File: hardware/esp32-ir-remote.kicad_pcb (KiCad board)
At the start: 2 copper layers, 65 parts, among them J1 ESP32-WROOM-32E-Breakout, J2 USB_C_Receptacle_USB2.0_14P, Q1 Q_NPN_BCE, Q2 Q_NPN_BCE, Q3 IRLML6344, Q4 2N7002, Q5 2N7002, SW1 RESET, SW2 BOOT, U1 AP63203WU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

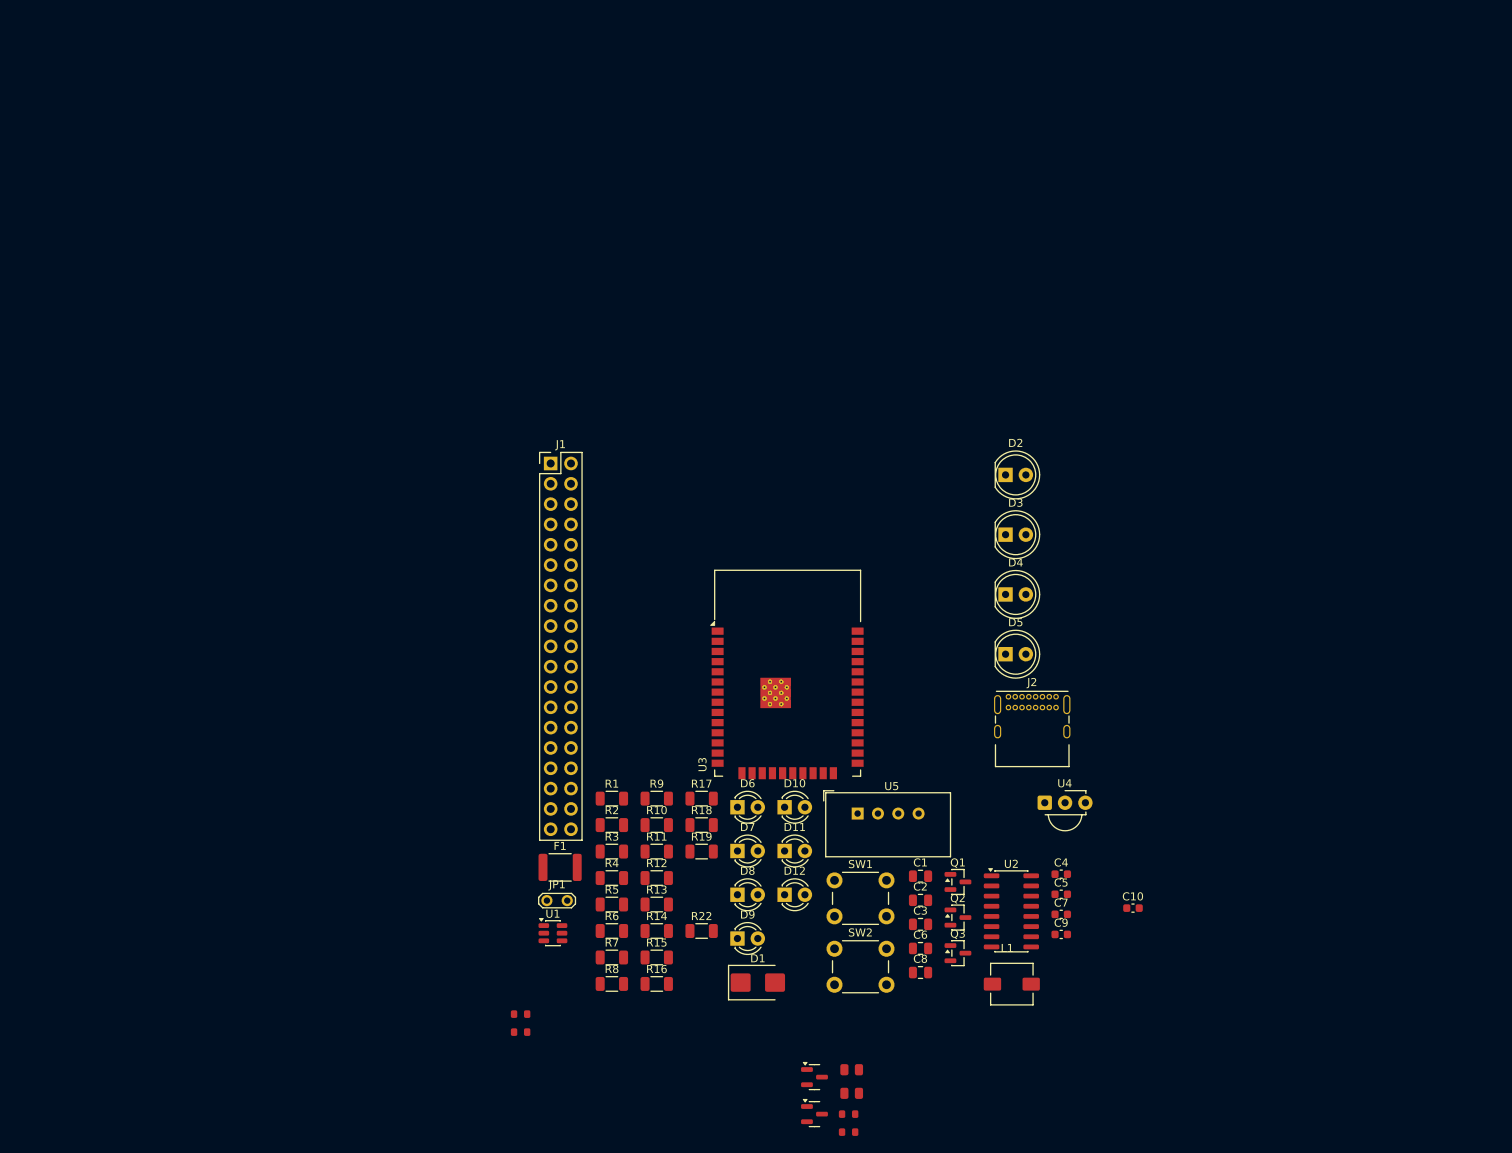
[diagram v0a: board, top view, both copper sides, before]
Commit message: H2.0: sync v1.2 schematic into PCB - footprints, values, nets all verified
- sync_schematic_to_board added J3-J6 + R27-R30 footprints and the v1.2 nets,
  but left J1 in place, kept stale footprints/values, and SPLIT the 7
  dual-labelled GPIO nets (U3 pads on ESP_GPIOxx vs peripherals on functional
  names) - all repaired:
- J1 (38-pin DevKitC breakout) deleted from board
- Footprint swaps via pcbnew (position/orientation/path/nets preserved):
  L1 -> lib:IND-SMD_L6.7-W6.7 (4.7uH), Q4/Q5 -> SOT-23,
  R20/R25 -> R_0805_2012Metric, R21/R23/R24/R26 -> R_0603_1608Metric
- Values: R13 10k->470R, R16 150R->470R, L1 3.9uH->4.7uH (H1.4 fixes)
- Net repairs: U3 GPIO pads rejoined to USER_LED1/2, TEMP_DATA, IR_TX, IR_RX,
  UART_TX/RX; U4/3 PWR_FLAG->IR_RX_VS; EXT_IR_A assigned to J5/1+R30/2;
  C7/C8 pad polarity matched to schematic
- lib/IND-SMD_L6.7-W6.7.kicad_mod: 4 graphics had (layer "") -> F.Fab
  (empty layer mapped to Rescue and broke headless LoadBoard)
- Machine-verified: net partition comparison netlist vs PCB = IDENTICAL
  (56 multi-node nets); 72/72 components match on footprint+value
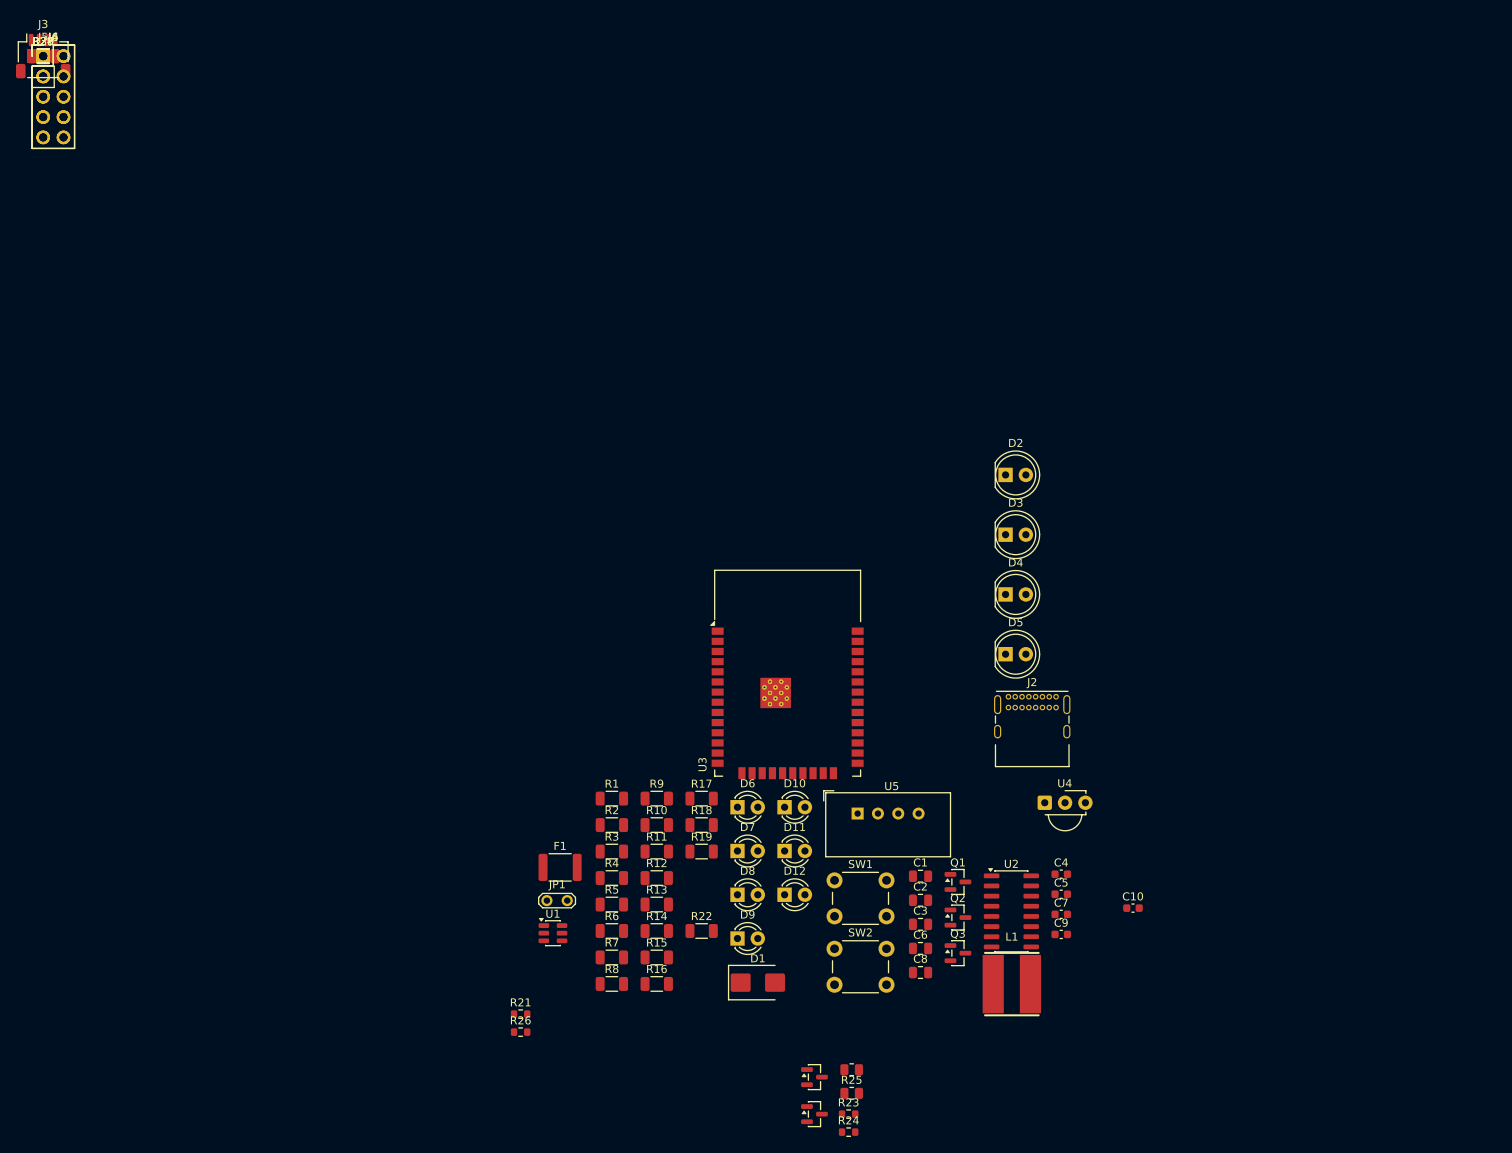
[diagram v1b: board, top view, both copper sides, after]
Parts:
- removed J1: ESP32-WROOM-32E-Breakout, lib:PinHeader_2x19_P2.54mm_DevKitC
- added J3: Qwiic_I2C, Connector_JST:JST_SH_SM04B-SRSS-TB_1x04-1MP_P1.00mm_Horizontal, F.Cu at (0.00, 0.00)
- added J4: GPIO_PWR, Connector_PinHeader_2.54mm:PinHeader_2x05_P2.54mm_Vertical, F.Cu at (0.00, 0.00)
- added J5: EXT_IR, Connector_PinHeader_2.54mm:PinHeader_1x02_P2.54mm_Vertical, F.Cu at (0.00, 0.00)
- added J6: JTAG, Connector_PinHeader_2.54mm:PinHeader_2x05_P2.54mm_Vertical, F.Cu at (0.00, 0.00)
- added R27: 100Ω, Resistor_SMD:R_1206_3216Metric, F.Cu at (0.00, 0.00)
- added R28, R29: 4.7kΩ, Resistor_SMD:R_1206_3216Metric, F.Cu at (0.00, 0.00)
- added R30: 18Ω, Resistor_SMD:R_1206_3216Metric, F.Cu at (0.00, 0.00)
- L1: value 3.9µH -> 4.7µH; footprint lib:INDM5752X300N -> lib:IND-SMD_L6.7-W6.7
- Q4, Q5: footprint PCM_JLCPCB:Q_SOT-23 -> Package_TO_SOT_SMD:SOT-23
- R13: value 10kΩ -> 470Ω
- R16: value 150Ω -> 470Ω
- R20, R25: footprint PCM_JLCPCB:R_0805 -> Resistor_SMD:R_0805_2012Metric
- R21, R23, R24, R26: footprint PCM_JLCPCB:R_0603 -> Resistor_SMD:R_0603_1608Metric
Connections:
- net /ESP_EN renamed ESP_EN
- net /ESP_GPIO0 renamed ESP_GPIO0
- net /ESP_GPIO1 renamed UART_TX
- net /ESP_GPIO15 renamed ESP_GPIO15
- net /ESP_GPIO16 renamed USER_LED1
- net /ESP_GPIO17 renamed USER_LED2
- net /ESP_GPIO18 renamed IR_TX
- net /ESP_GPIO19 renamed IR_RX
- net /ESP_GPIO2 renamed ESP_GPIO2
- net /ESP_GPIO3 renamed UART_RX
- net /ESP_GPIO4 renamed TEMP_DATA
- net /USB_D+ renamed USB_D+
- net /USB_D- renamed USB_D-
- net Net-(D2-K) renamed IR_DRAIN
- C9 pad 1: +3.3V -> IR_RX_VS
- U3 pad 10: /ESP_GPIO25 -> ESP_GPIO25
- U3 pad 11: /ESP_GPIO26 -> ESP_GPIO26
- U3 pad 13: /ESP_GPIO14 -> ESP_GPIO14
- U3 pad 14: /ESP_GPIO12 -> ESP_GPIO12
- U3 pad 16: /ESP_GPIO13 -> ESP_GPIO13
- U3 pad 33: /ESP_GPIO21 -> ESP_GPIO21
- U3 pad 36: /ESP_GPIO22 -> ESP_GPIO22
- U3 pad 37: /ESP_GPIO23 -> ESP_GPIO23
- U3 pad 6: /ESP_GPIO34 -> ESP_GPIO34
- U3 pad 8: /ESP_GPIO32 -> ESP_GPIO32
- U3 pad 9: /ESP_GPIO33 -> ESP_GPIO33
- U4 pad 3: +3.3V -> IR_RX_VS

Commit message: H2.2: board outline 80x55 + full placement, zero courtyard overlaps
- Outline (100,60)-(180,115) with 4x M3 NPTH mounting holes (H1 pulled east
  of the WROOM antenna courtyard wedge; H3/H4 in corners)
- All 76 footprints placed per hardware/notes/layout.md zones:
  WROOM antenna overhangs west edge 1.5mm; IR fan D2-D5 north edge rotated
  -67.5/-22.5/+22.5/+67.5 with R9-R12 row behind; TSOP+RC NE corner facing
  east; DHT22 + Qwiic + spare header east; USB-C south-center (mouth
  overhang fixed - courtyard is offset 2mm from origin, was recessed 1.9mm);
  buck cluster SW clear of the antenna keepout strip; CH340C between USB and
  module; status-LED bar D6-D9 along south-west edge; user LEDs D11/D12 +
  drivers by the buttons; JTAG J6 (DNP) center-east
- R<->LED affinities placed from netlist connectivity (D6:R15 D7:R16 D8:R17
  D9:R18 D10:R19 - corrected from earlier guesses)
- Verified: polygon-exact courtyard intersection = 0 overlaps; all
  courtyards inside outline except deliberate overhangs (U3/J2/J3/U4)
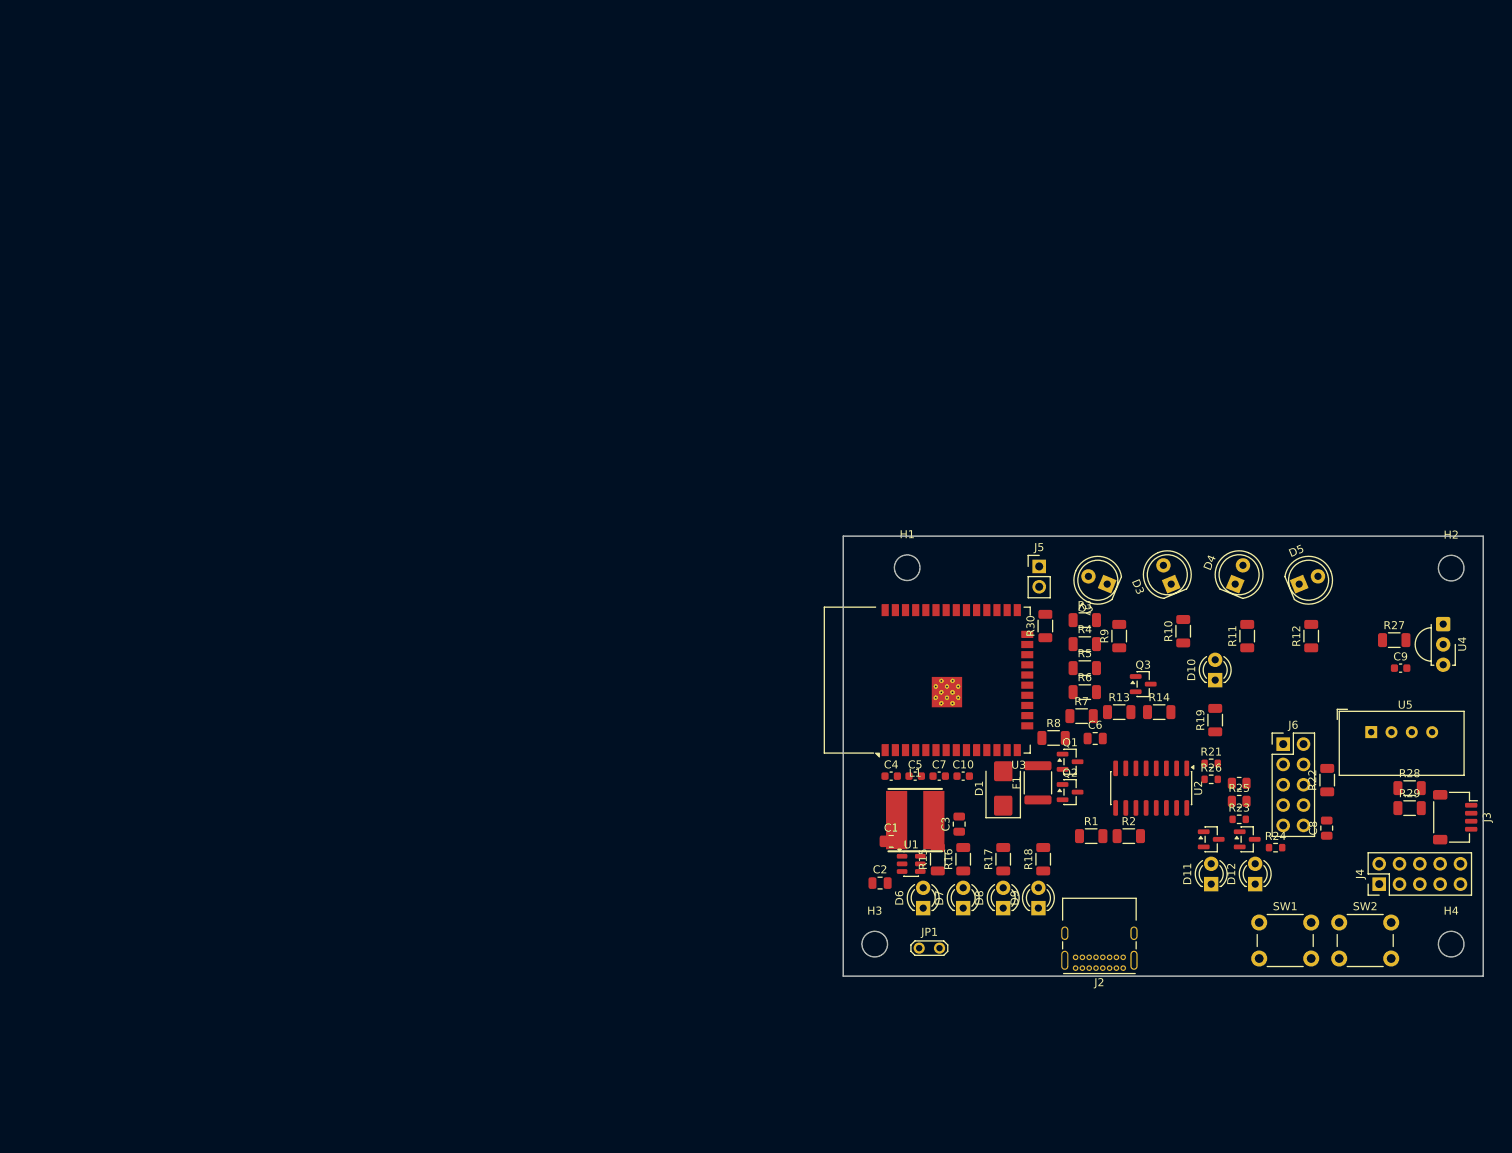
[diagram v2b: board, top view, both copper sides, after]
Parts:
- added H1: M3, MountingHole:MountingHole_3.2mm_M3, F.Cu at (108.0, 63.9)
- added H2: M3, MountingHole:MountingHole_3.2mm_M3, F.Cu at (176.0, 64.0)
- added H3: M3, MountingHole:MountingHole_3.2mm_M3, F.Cu at (103.9, 111.0)
- added H4: M3, MountingHole:MountingHole_3.2mm_M3, F.Cu at (176.0, 111.0)
- moved J3 200.5 mm to (176.5, 95.1), turned to -90 degrees
- moved J4 196.5 mm to (167.0, 103.5), turned to 90 degrees
- moved R29 195.0 mm to (170.8, 94.0)
- moved R28 193.8 mm to (170.8, 91.5)
- moved R27 184.0 mm to (168.9, 73.0)
- moved J6 177.3 mm to (155.0, 86.0)
- moved R30 144.1 mm to (125.3, 71.2), turned to 90 degrees
- moved J5 139.9 mm to (124.5, 63.8)
- moved R26 91.9 mm to (146.0, 90.4)
- moved R21 91.8 mm to (146.0, 88.4)
- moved R12 87.2 mm to (158.5, 72.5), turned to 90 degrees
- moved R22 80.4 mm to (160.5, 90.5), turned to 90 degrees
- moved R11 78.6 mm to (150.5, 72.5), turned to 90 degrees
- moved R10 70.1 mm to (142.5, 71.9), turned to 90 degrees
- moved R14 68.5 mm to (139.5, 82.0)
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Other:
- board outline added: 80 x 55 mm

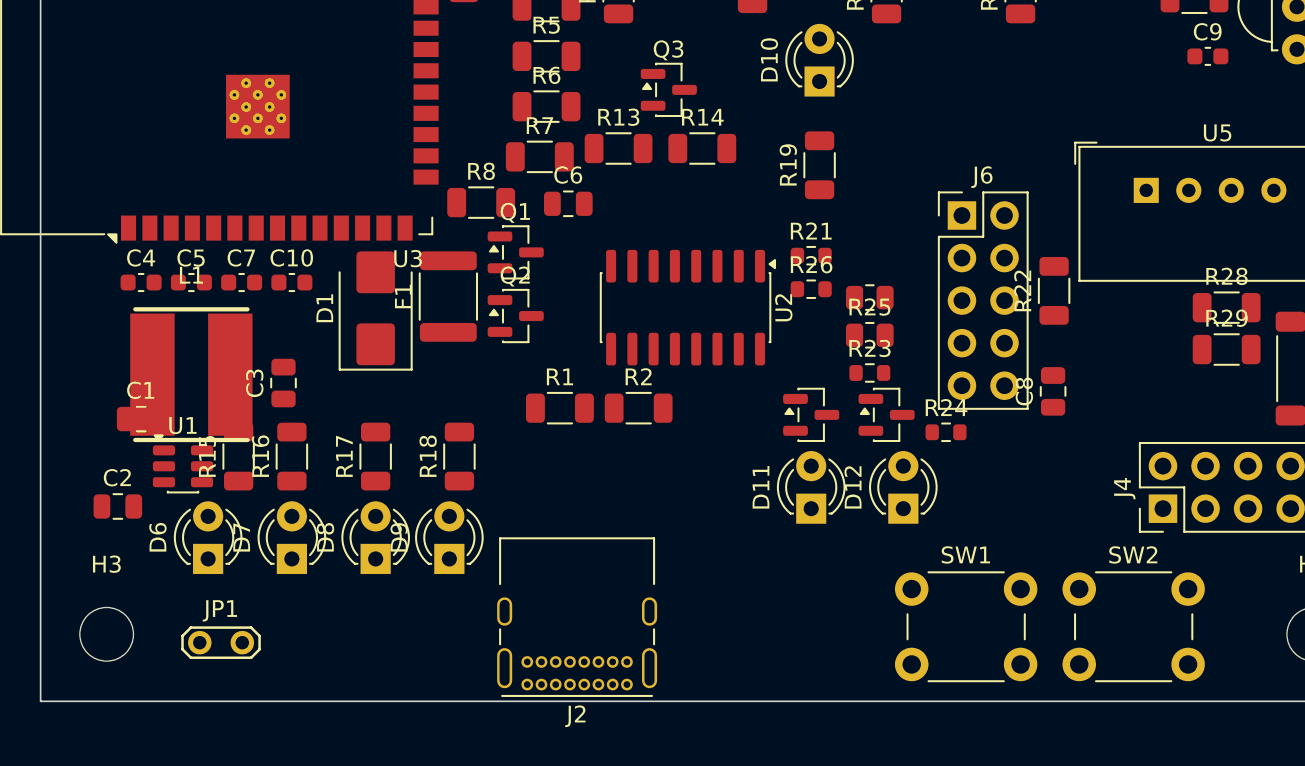
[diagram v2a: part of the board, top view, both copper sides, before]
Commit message: Fix BOM blockers found by adversarial LCSC validation (pre-routing)
Subagent validated all 35 LCSC codes against the live catalog; findings fixed:
- BLOCKER: Q1/Q2 used Q_NPN_BCE symbol but S8050 (C2146) SOT-23 is B-E-C -
  collector/emitter were swapped on the physical part (auto-reset would not
  work). Embedded symbol pin numbers swapped -> Q_NPN_BEC, wires untouched,
  netlist nodes confirm C: pad2->3, E: pad3->2; PCB pad nets swapped to match.
- BLOCKER: SW1/SW2 carried SMD switch code C455280 (TS-1088R 4x3mm) on a THT
  6mm footprint - unassemblable. Footprint -> JLC-MCP:SW-SMD_L3.9-W3.0-P4.45
  (fetched via jlcpcb MCP, validated 2 pads, clean layers); now SMT-line
  assemblable.
- HIGH: R9-R12+R30 carried C17955 = 20 ohm, not 18 - IR drive current 10% low.
  -> C17922 (18 ohm 1206 1% 250mW, Extended accepted: power margin per
  ir-transmitter.md needs 1206/0.25W).
- HIGH: 0805 codes on 1206 footprints: R3-R8+R22 -> C17902 (10k 1206 Basic);
  R1/R2 + R13/R16-R19 -> footprints to R_0805 keeping Basic 0805 codes
  (no Basic 1206 exists for 5.1k/470R).
- HIGH: JP1 testpoint (0.8mm drills) had pin-header code C124375 that cannot
  fit - code removed; JP1 is a solder-bridge/test-point, no part.
- Noted for order time: AM2302 stock critically low (37 units).

Verified: ERC 0 errors; netlist partition PCB==schematic identical;
footprint/value match 72/72; courtyard overlaps 0. BOM CSV regenerated.
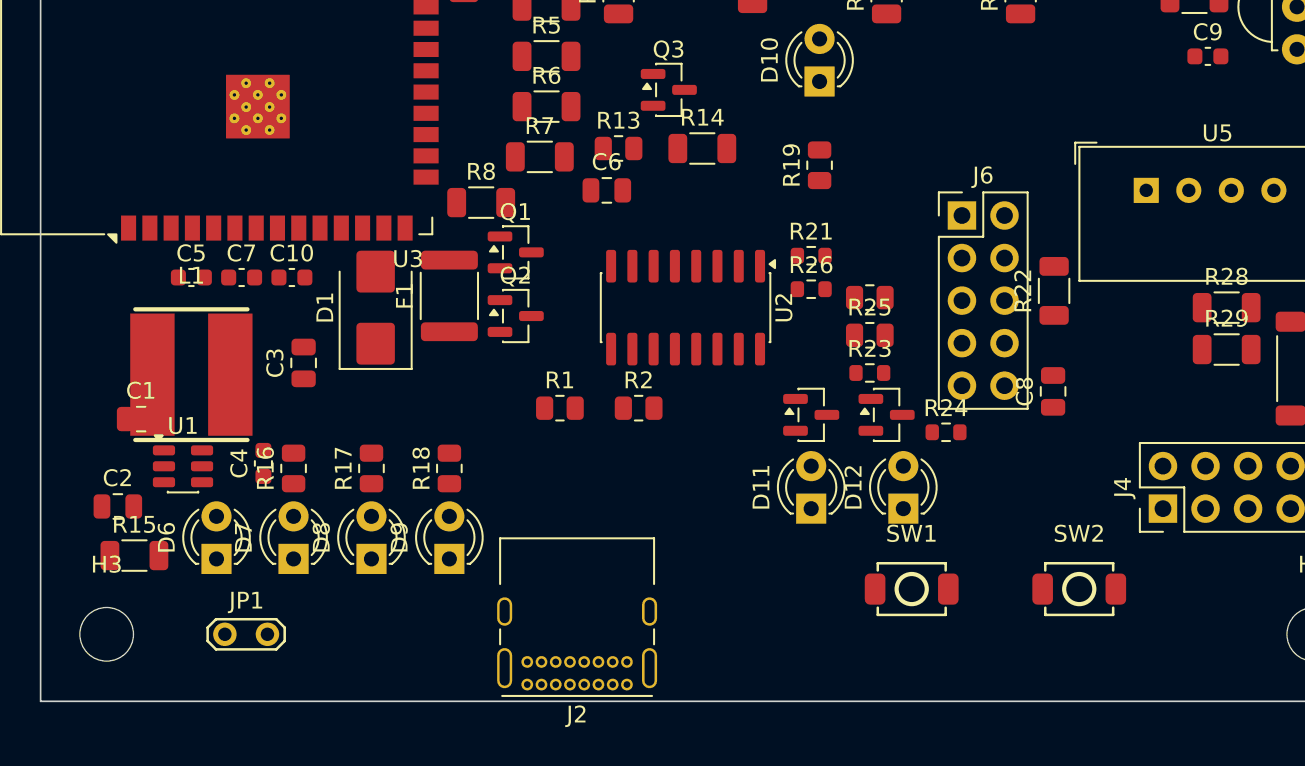
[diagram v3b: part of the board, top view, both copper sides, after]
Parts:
- R1, R13, R16, R17, R18, R19, R2: footprint Resistor_SMD:R_1206_3216Metric -> Resistor_SMD:R_0805_2012Metric
- SW1, SW2: footprint Button_Switch_THT:SW_PUSH_6mm -> JLC-MCP:SW-SMD_L3.9-W3.0-P4.45
- moved C4 13.0 mm to (113.3, 100.8), turned to 90 degrees
- moved R15 8.58 mm to (105.6, 106.3), turned to 0 degrees
- moved C6 2.44 mm to (133.8, 84.5)
- moved C3 1.70 mm to (115.7, 94.8)
- moved JP1 1.58 mm to (111.0, 111.0)
- moved R18 0.93 mm to (124.4, 101.1)
- moved R17 0.75 mm to (119.8, 101.1)
- moved R16 0.72 mm to (115.1, 101.1)
- moved D6 0.50 mm to (110.5, 106.5)
- moved C10 0.30 mm to (115.0, 89.7)
- moved C5 0.30 mm to (109.0, 89.7)
- moved C7 0.30 mm to (112.0, 89.7)
- moved D8 0.25 mm to (119.8, 106.5)
- moved D7 0.10 mm to (115.1, 106.5)
- moved F1 0.07 mm to (124.4, 90.8)
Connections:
- Q1 pad 2: ESP_EN -> Net-(Q1-E)
- Q1 pad 3: Net-(Q1-E) -> ESP_EN
- Q2 pad 2: ESP_GPIO0 -> Net-(Q2-E)
- Q2 pad 3: Net-(Q2-E) -> ESP_GPIO0
